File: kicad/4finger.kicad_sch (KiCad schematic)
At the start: 39 parts, among them J9 Conn_01x10_Pin, SW10 SW_PUSH, SW11 SW_PUSH, SW12 SW_PUSH, SW13 SW_PUSH, SW14 SW_PUSH, SW15 SW_PUSH, SW16 SW_PUSH, SW17 SW_PUSH, SW18 SW_PUSH, SW19 SW_PUSH, SW20 SW_PUSH, SW21 SW_PUSH, SW22 SW_PUSH, SW23 SW_PUSH, SW24 SW_PUSH, SW25 SW_PUSH, SW7 SW_PUSH, SW8 SW_PUSH, SW9 SW_PUSH

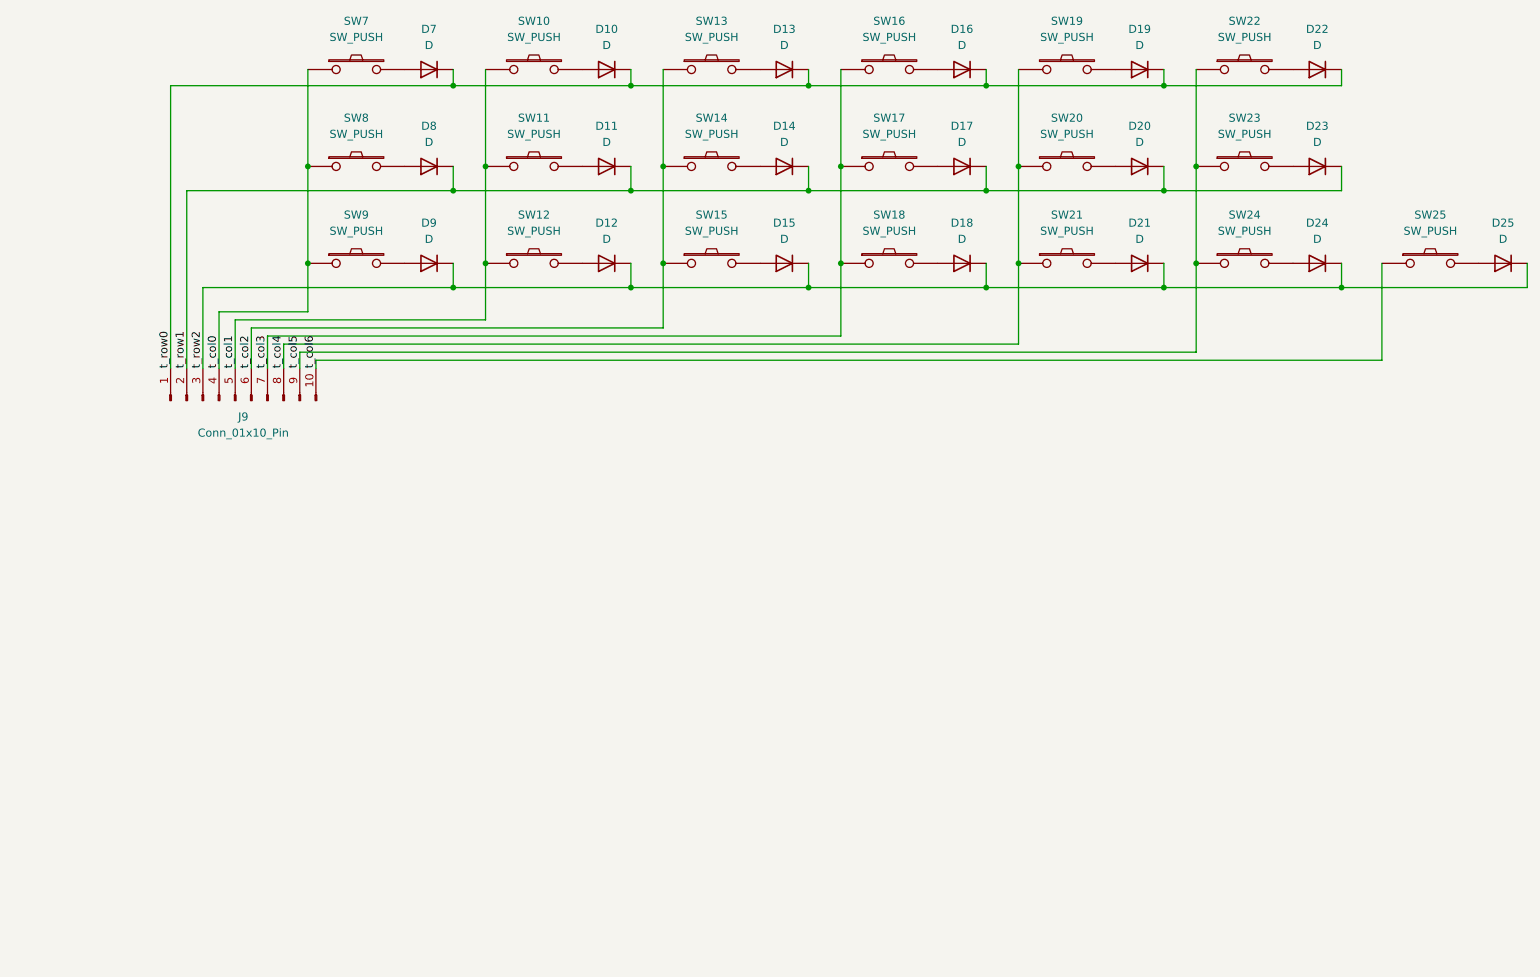
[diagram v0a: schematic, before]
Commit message: Add LEDs, and convert RP2040 to SMD
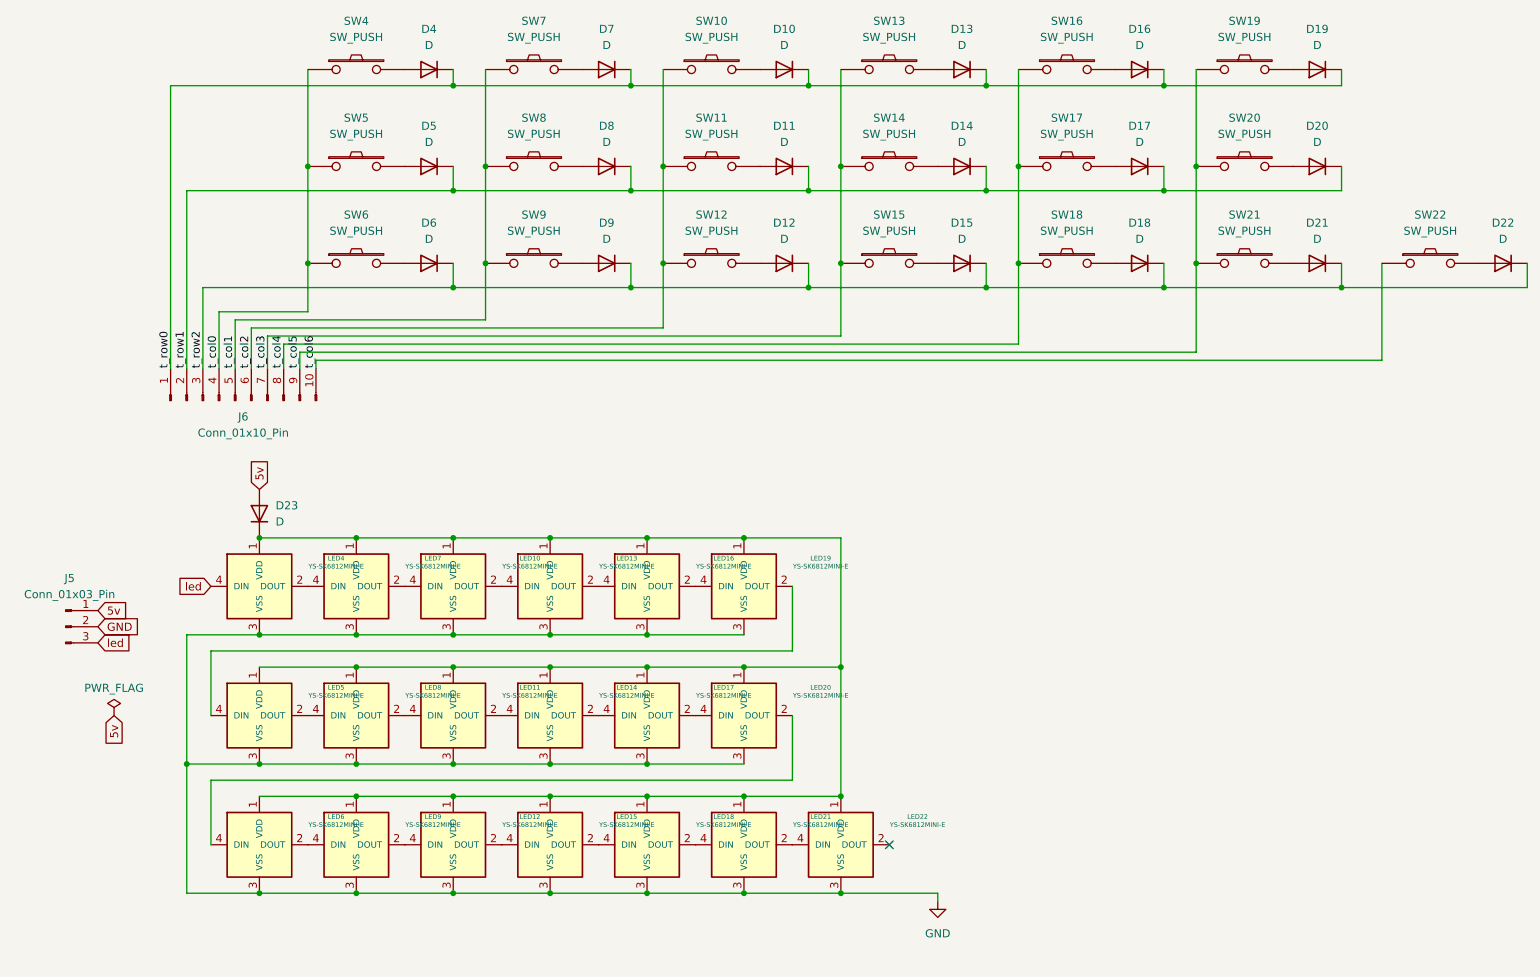
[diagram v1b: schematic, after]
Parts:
- added D23: D, kbd:D3_SMD, symbol Device:D
- added J5: Conn_01x03_Pin, Connector_PinHeader_2.54mm:PinHeader_1x03_P2.54mm_Vertical, symbol Connector:Conn_01x03_Pin
- added LED10, LED11, LED12, LED13, LED14, LED15, LED16, LED17, LED18, LED19, LED20, LED21, LED22, LED4, LED5, LED6, LED7, LED8, LED9: YS-SK6812MINI-E, sepsepkbd:YS-SK6812MINI-E, symbol kbd:YS-SK6812MINI-E
- renumbered D13 to D10, D14 to D11, D15 to D12, D16 to D13, D17 to D14, D18 to D15, D19 to D16, D20 to D17, D21 to D18, D22 to D19, D23 to D20, D24 to D21, D25 to D22, D7 to D4, D8 to D5, D9 to D6, D10 to D7, D11 to D8, D12 to D9, J9 to J6, SW13 to SW10, SW14 to SW11, SW15 to SW12, SW16 to SW13, SW17 to SW14, SW18 to SW15, SW19 to SW16, SW20 to SW17, SW21 to SW18, SW22 to SW19, SW23 to SW20, SW24 to SW21, SW25 to SW22, SW7 to SW4, SW8 to SW5, SW9 to SW6, SW10 to SW7, SW11 to SW8, SW12 to SW9
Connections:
- new net: D23.1 (K), LED10.1 (VDD), LED11.1 (VDD), LED12.1 (VDD), LED13.1 (VDD), LED14.1 (VDD), LED15.1 (VDD), LED16.1 (VDD), LED17.1 (VDD), LED18.1 (VDD), LED19.1 (VDD), LED20.1 (VDD), LED21.1 (VDD), LED22.1 (VDD), LED4.1 (VDD), LED5.1 (VDD), LED6.1 (VDD), LED7.1 (VDD), LED8.1 (VDD), LED9.1 (VDD)
- new net: LED13.2 (DOUT), LED16.4 (DIN)
- new net: LED10.2 (DOUT), LED13.4 (DIN)
- new net: LED4.2 (DOUT), LED7.4 (DIN)
- new net: LED20.2 (DOUT), LED6.4 (DIN)
- new net: LED17.2 (DOUT), LED20.4 (DIN)
- new net: LED6.2 (DOUT), LED9.4 (DIN)
- new net: LED15.2 (DOUT), LED18.4 (DIN)
- new net: LED12.2 (DOUT), LED15.4 (DIN)
- new net: LED12.4 (DIN), LED9.2 (DOUT)
- new net: LED5.2 (DOUT), LED8.4 (DIN)
- new net: LED19.2 (DOUT), LED5.4 (DIN)
- new net: LED16.2 (DOUT), LED19.4 (DIN)
- new net: LED11.2 (DOUT), LED14.4 (DIN)
- new net: LED11.4 (DIN), LED8.2 (DOUT)
- new net: LED10.4 (DIN), LED7.2 (DOUT)
- new net: LED18.2 (DOUT), LED21.4 (DIN)
- new net: LED14.2 (DOUT), LED17.4 (DIN)
- new net: LED21.2 (DOUT), LED22.4 (DIN)
- new net 5v: D23.2 (A), J5.1 (Pin_1)
- new net GND: J5.2 (Pin_2), LED10.3 (VSS), LED11.3 (VSS), LED12.3 (VSS), LED13.3 (VSS), LED14.3 (VSS), LED15.3 (VSS), LED16.3 (VSS), LED17.3 (VSS), LED18.3 (VSS), LED19.3 (VSS), LED20.3 (VSS), LED21.3 (VSS), LED22.3 (VSS), LED4.3 (VSS), LED5.3 (VSS), LED6.3 (VSS), LED7.3 (VSS), LED8.3 (VSS), LED9.3 (VSS)
- new net led: J5.3 (Pin_3), LED4.4 (DIN)
- no-connect marks 0 -> 1

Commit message: 2.1
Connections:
- net 5v renamed t_5v
- net GND renamed t_GND
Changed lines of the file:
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@@
 		)
 	)
-	(global_label "5v"
+	(global_label "t_5v"
 		(shape input)
 		(at 60.96 97.79 90)
@@
 		)
 		(property "Intersheetrefs" "${INTERSHEET_REFS}"
-			(at 60.96 92.6277 90)
+			(at 60.96 90.9344 90)
 			(effects
 				(font
@@
 		)
 	)
-	(global_label "5v"
+	(global_label "t_5v"
 		(shape input)
 		(at 35.56 116.84 0)
@@
 		)
 		(property "Intersheetrefs" "${INTERSHEET_REFS}"
-			(at 40.7223 116.84 0)
+			(at 42.4156 116.84 0)
 			(effects
 				(font
@@
 		)
 	)
-	(global_label "5v"
+	(global_label "t_5v"
 		(shape input)
 		(at 38.1 133.35 270)
@@
 		)
 		(property "Intersheetrefs" "${INTERSHEET_REFS}"
-			(at 38.1 138.5123 90)
+			(at 38.1 140.2056 90)
 			(effects
 				(font
@@
 		)
 	)
-	(global_label "GND"
+	(global_label "t_GND"
 		(shape input)
-		(at 35.56 119.38 0)
+		(at 167.64 162.56 270)
 		(fields_autoplaced yes)
 		(effects
@@
 				(size 1.27 1.27)
 			)
+			(justify right)
+		)
+		(property "Intersheetrefs" "${INTERSHEET_REFS}"
+			(at 167.64 171.109 90)
+			(effects
+				(font
+					(size 1.27 1.27)
+				)
+				(justify right)
+				(hide yes)
+			)
+		)
+	)
+	(global_label "t_GND"
+		(shape input)
+		(at 35.56 119.38 0)
+		(fields_autoplaced yes)
+		(effects
+			(font
+				(size 1.27 1.27)
+			)
 			(justify left)
 		)
 		(property "Intersheetrefs" "${INTERSHEET_REFS}"
-			(at 42.4157 119.38 0)
+			(at 44.109 119.38 0)
 			(effects
 				(font
@@
 					(unit 1)
 				)
-			)
-		)
-	)
-	(symbol
-		(lib_id "power:GND")
-		(at 167.64 162.56 0)
-		(unit 1)
-		(exclude_from_sim no)
-		(in_bom yes)
-		(on_board yes)
-		(dnp no)
-		(fields_autoplaced yes)
-		(property "Reference" "#PWR07"
-			(at 167.64 168.91 0)
-			(effects
-				(font
-					(size 1.27 1.27)
-				)
-				(hide yes)
-			)
-		)
-		(property "Value" "GND"
-			(at 167.64 167.64 0)
-			(effects
-				(font
-					(size 1.27 1.27)
-				)
-			)
-		)
-		(property "Footprint" ""
-			(at 167.64 162.56 0)
-			(effects
-				(font
-					(size 1.27 1.27)
-				)
-				(hide yes)
-			)
-		)
-		(property "Datasheet" ""
-			(at 167.64 162.56 0)
-			(effects
-				(font
-					(size 1.27 1.27)
-				)
-				(hide yes)
-			)
-		)
-		(property "Description" "Power symbol creates a global label with name \"GND\" , ground"
-			(at 167.64 162.56 0)
-			(effects
-				(font
-					(size 1.27 1.27)
-				)
-				(hide yes)
-			)
-		)
-		(pin "1"
-		)
-		(instances
-			(project "sepsepkbd"
-				(path "/eb7c7458-55fc-48e8-93c5-5460ac0da007/df87ea1b-53aa-46ba-a1ff-8fb7fc109e39"
-					(reference "#PWR07")
-					(unit 1)
-				)

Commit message: additional silk on both sides
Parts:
- J5: footprint Connector_PinHeader_2.54mm:PinHeader_1x03_P2.54mm_Vertical -> sepsepkbd:PinHeader_1x03_P2.54mm_Vertical
- J6: footprint Connector_PinHeader_2.54mm:PinHeader_1x10_P2.54mm_Vertical -> sepsepkbd:PinHeader_1x10_P2.54mm_Vertical
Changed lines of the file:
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@@
 			)
 		)
-		(property "Footprint" "Connector_PinHeader_2.54mm:PinHeader_1x10_P2.54mm_Vertical"
+		(property "Footprint" "sepsepkbd:PinHeader_1x10_P2.54mm_Vertical"
 			(at 57.15 83.82 0)
 			(effects
@@
 			)
 		)
-		(property "Footprint" "Connector_PinHeader_2.54mm:PinHeader_1x03_P2.54mm_Vertical"
+		(property "Footprint" "sepsepkbd:PinHeader_1x03_P2.54mm_Vertical"
 			(at 30.48 119.38 0)
 			(effects
